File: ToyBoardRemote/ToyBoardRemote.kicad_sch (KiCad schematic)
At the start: 23 parts, among them Q1 NMOS, SW1 SW_Push, SW2 SW_Push, SW3 SW_Push, SW4 SW_Push, SW5 SW_Push

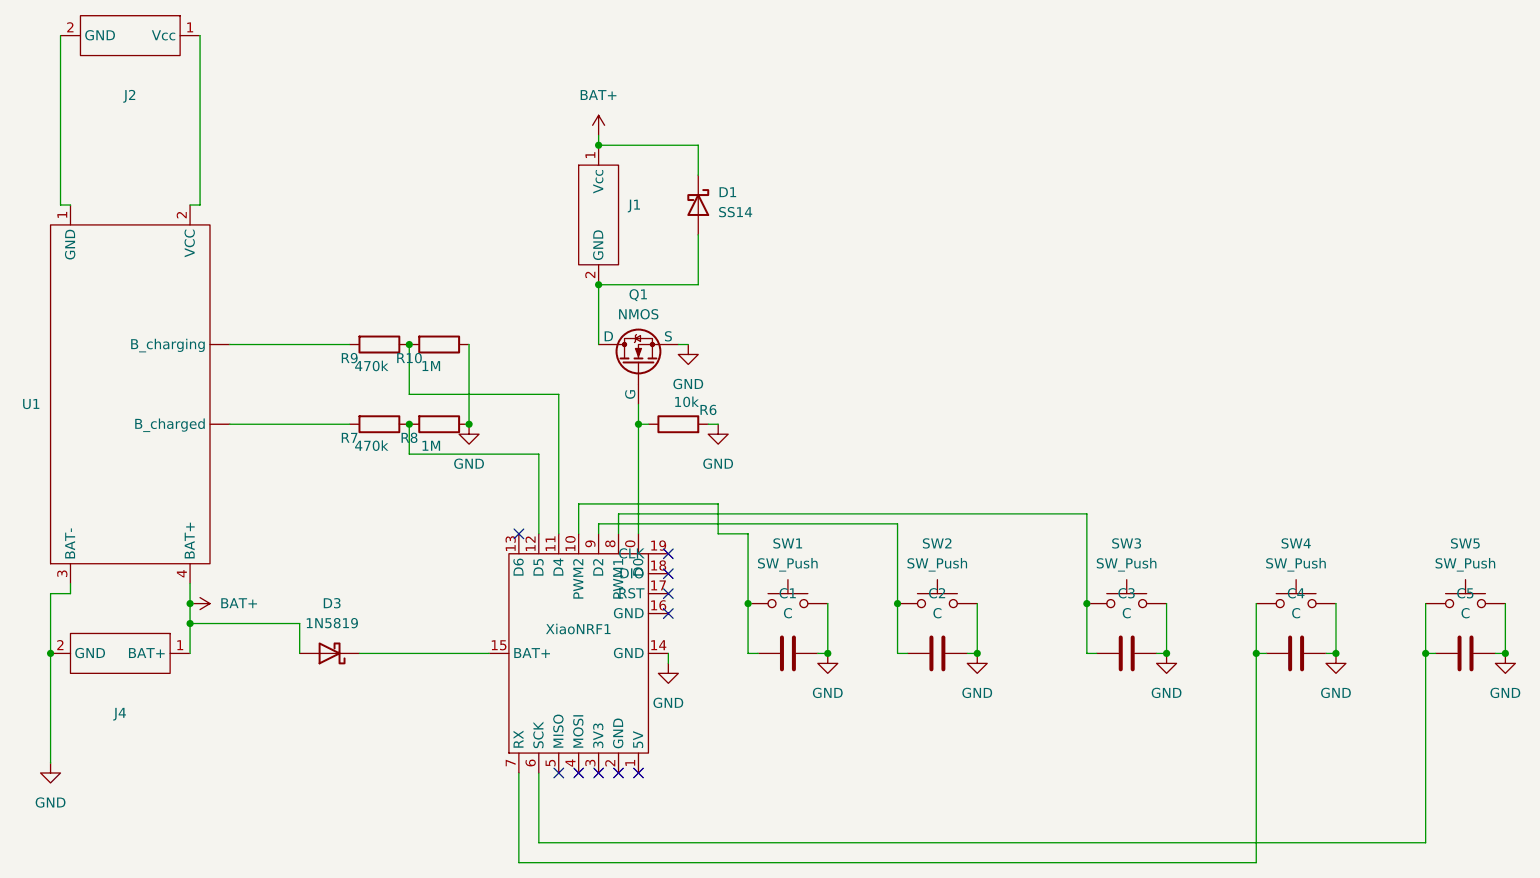
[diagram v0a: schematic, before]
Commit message: cleaner schematic
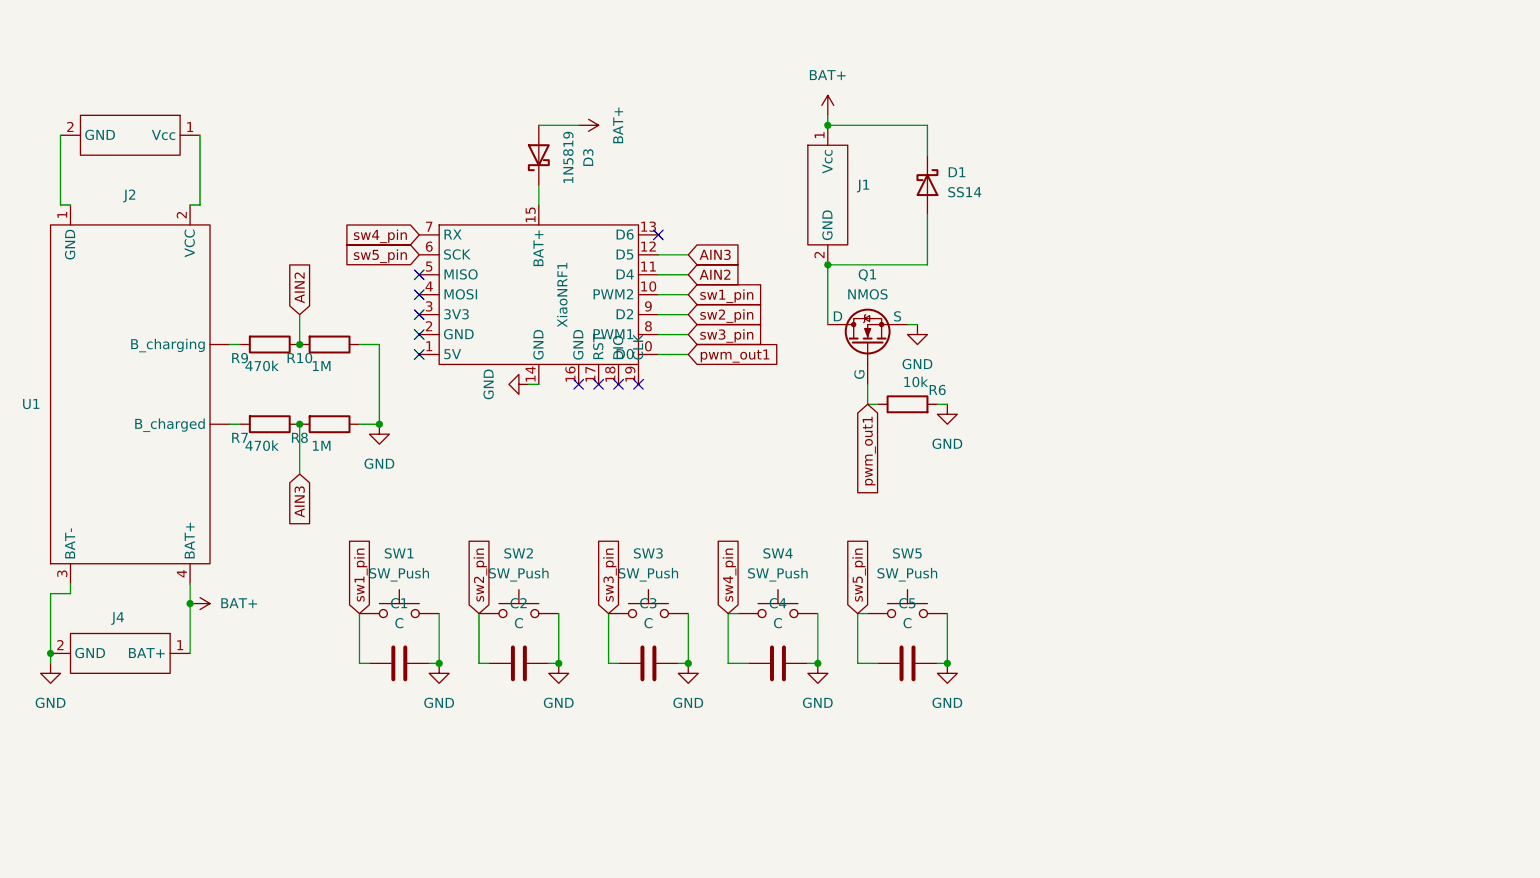
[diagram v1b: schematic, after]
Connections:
- net pwm_out1: now reaches Q1.2 (G), R6.1, XiaoNRF1.0 (D0)
- net sw4_pin: now reaches C4.2, SW4.1, XiaoNRF1.7 (RX)
- net sw1_pin: now reaches C1.2, SW1.1, XiaoNRF1.10 (PWM2)
- net AIN2: now reaches R10.2, R9.1, XiaoNRF1.11 (D4)
- net AIN3: now reaches R7.1, R8.2, XiaoNRF1.12 (D5)
- net sw5_pin: now reaches C5.2, SW5.1, XiaoNRF1.6 (SCK)
- net sw3_pin: now reaches C3.2, SW3.1, XiaoNRF1.8 (PWM1)
- net sw2_pin: now reaches C2.2, SW2.1, XiaoNRF1.9 (D2)
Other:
- moved on the sheet: C1, C2, C3, C4, C5, D1, D3, J1, J2, Q1, R10, R6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
